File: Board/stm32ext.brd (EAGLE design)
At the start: 0 parts

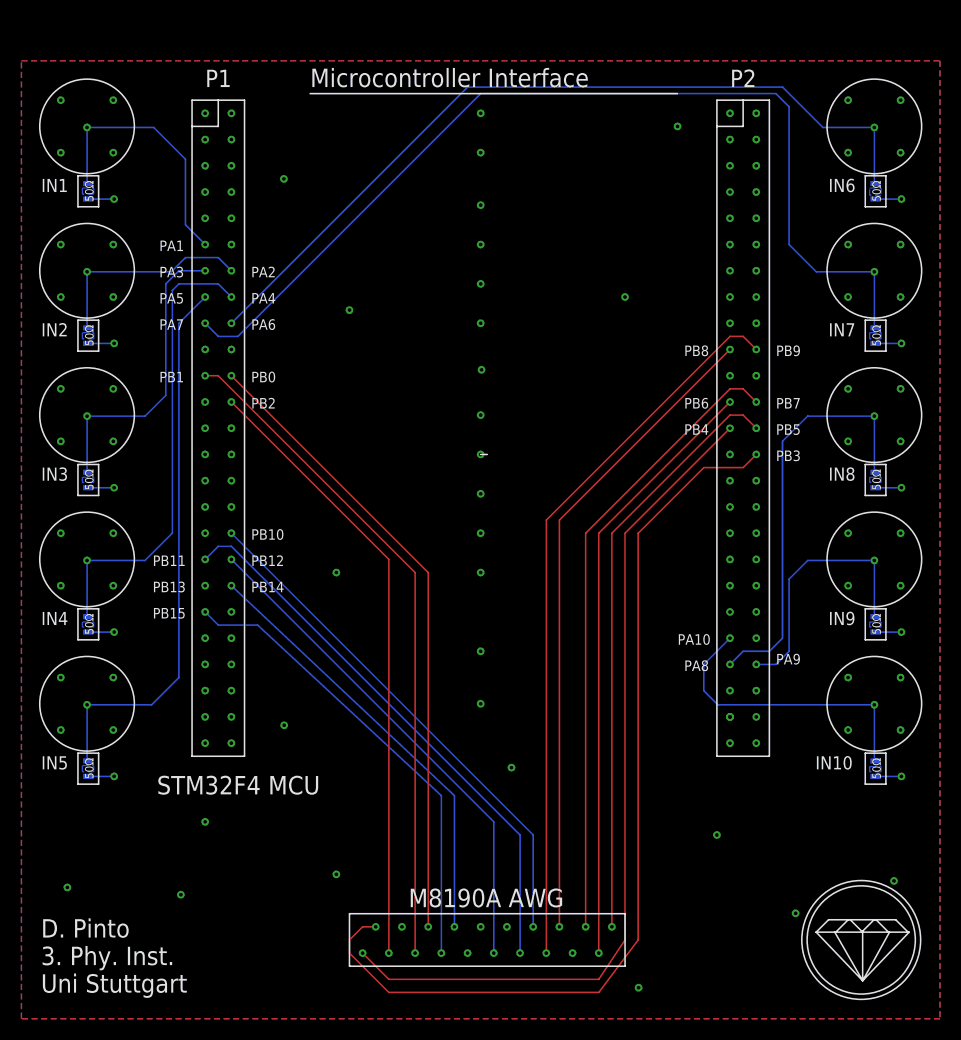
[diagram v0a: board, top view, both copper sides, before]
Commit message: Fixed drill size (partially.)
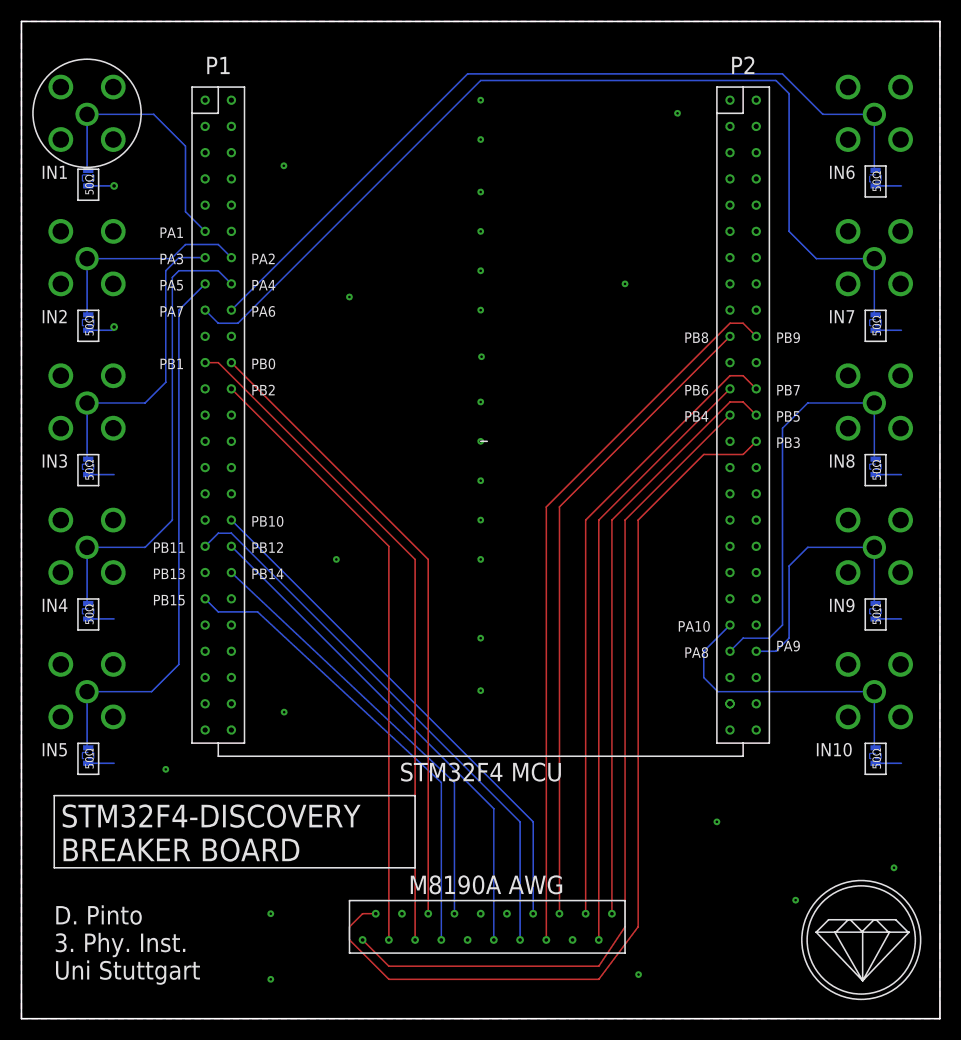
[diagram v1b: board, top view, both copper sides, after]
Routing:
- net S$4: vias 1 -> 0
- net S$16: vias 1 -> 0
- net S$18: vias 1 -> 0
- net S$9: vias 1 -> 0
- net S$6: vias 1 -> 0
- net S$19: vias 1 -> 0
- net S$17: vias 1 -> 0
- net S$10: vias 1 -> 0
- net S$1: vias 1 -> 0
- net GND: vias 93 -> 80
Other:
- board outline added: 88.9 x 96.5 mm
- board text added: "STM32F4-DISCOVERY BREAKER BOARD"
- board text removed: "Microcontroller Interface"
